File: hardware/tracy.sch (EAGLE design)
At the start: 62 parts, among them IC1 SIM900, J1 U.FL, Q1 si2305cd, Q2 8MHz 18pF, Q3 IRFR5305, T1 BC846, U1 SPX5205 3v3, X3 MKDSN1,5/4-5,08, Y1 32768Hz CFPX-217 12.5pF

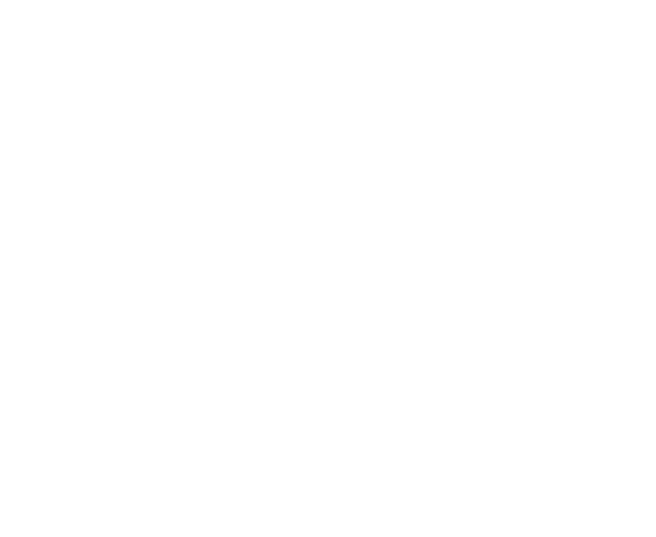
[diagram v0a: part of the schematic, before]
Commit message: create sim card reader footprint
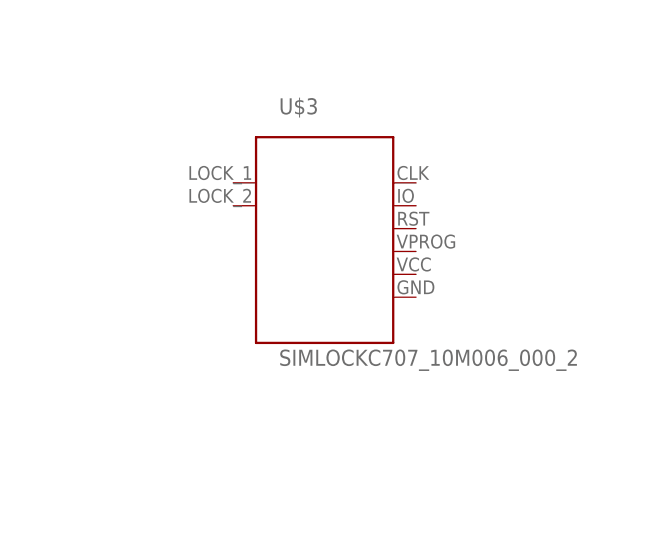
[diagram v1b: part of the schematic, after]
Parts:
- added U$3: SIMLOCKC707_10M006_000_2, Simplex-Connectors:SIMLOCKC707_10M006_000_2
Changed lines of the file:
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@@
 <part name="GND8" library="SparkFun" deviceset="GND" device=""/>
 <part name="IC1" library="sim900" deviceset="SIM900" device=""/>
+<part name="U$3" library="Simplex-Connectors" deviceset="SIMLOCK" device="C707_10M006_000_2"/>
 </parts>
 <sheets>
@@
 <instance part="GND8" gate="1" x="22.86" y="241.3"/>
 <instance part="IC1" gate="G$1" x="345.44" y="363.22"/>
+<instance part="U$3" gate="G$1" x="441.96" y="378.46"/>
 </instances>
 <busses>

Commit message: sch work
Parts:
- removed C15: 10uF, SparkFun-Capacitors:CAP_POLD
- removed C2, C20: 10uF, rcl:C-EUC1206
- removed C21, C22: 33pF, rcl:C-EUC0805
- removed D2: SB560, diode:DIODE-C1702-05
- removed JP1: i2c, SparkFun-Connectors:M04PTH
- removed JP2: thermistor, SparkFun-Connectors:M02PTH
- removed JP5: debug, SparkFun-Connectors:M07
- removed JP9: digital2, SparkFun-Connectors:M07
- removed LED1: green, led:LEDCHIP-LED0805
- removed LED2: orange, led:LEDCHIP-LED0805
- removed Q1: si2305cd, Simplex-DiscreteSemi:MOSFET-PCHANNELSMD_POWER
- removed Q2: 8MHz 18pF, Omat_komponentit:CRYTAL
- removed Q3: IRFR5305, transistor-power:IRFR5305
- removed R10, R27: 1K, rcl:R-EU_R0805W
- removed R12, R13: 320, rcl:R-EU_R0805W
- removed R16, R3: 100k, rcl:R-EU_R0805W
- removed R19, R8: 10k, rcl:R-EU_R0805W
- removed R25: 2M, rcl:R-EU_R0805W
- removed R26: 240k, rcl:R-EU_R0805W
- removed R4, R5, R6, R7: 4.7k, rcl:R-EU_R0805W
- removed T1: BC846, transistor:BC846
- removed U$4: INDUCTOR, Simplex-rlc:INDUCTOR
- removed X3: MKDSN1,5/4-5,08, con-phoenix-508:MKDSN1,5/4-5,08
- added C12: 4u7, rcl:C-EUC0805
- added C13: 100n, rcl:C-EUC0805
- added C14: 22p, rcl:C-EUC0805
- added C16: 47uF, rcl:C-EUC1206
- added C25, C26, C29: 100nF, rcl:C-EUC0805
- added C27, C28: 4u7, rcl:C-EUC1206
- added C30: 10uF, rcl:C-EUC1206
- added C32: 1uF, rcl:C-EUC0805
- added D1: DIODE-SCHOTTKY_, SparkFun-DiscreteSemi:DIODE-SCHOTTKY_
- added J2: U.FL, SparkFun-Connectors:U.FL
- added LED3: orange, led:LEDCHIP-LED0805
- added Q4: si2305cd, Simplex-DiscreteSemi:MOSFET-PCHANNELSMD_POWER
- added R11: 3k, rcl:R-EU_R0805W
- added R14: NA/10k, rcl:R-EU_R0805W
- added R15: 1k1, rcl:R-EU_R0805W
- added R17, R23, R9: 10k, rcl:R-EU_R0805W
- added R18: 47k, rcl:R-EU_R0805W
- added R20: 4k7, rcl:R-EU_R0805W
- added R21: 100k, rcl:R-EU_R0805W
- added T2: BC846, transistor:BC846
- added U$10: bead, Simplex-rlc:INDUCTOR
- added U$6: BQ24072, Simplex-ICs:BQ24072
- added U$8: 22, Simplex-rlc:RES_ARR
- added U$9: RESETTABLE, Simplex-Fuses:RESETTABLE
- added U3: TC1014 2V8, SparkFun:V_REG_LDOSMD
- C19: value 100nF -> 10uF; device rcl:C-EUC0805 -> rcl:C-EUC1206
- R2: value 10k -> 470
- U$2: value RESETTABLE -> 470; device Simplex-Fuses:RESETTABLE -> Simplex-rlc:RES_ARR
- U$5: value INDUCTOR -> bead
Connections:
- net CS renamed P4.6
- net MOSI renamed P4.1
- removed net EN: R8.1, U$1.20
- removed net LED: R10.2, U$1.36
- removed net MISO: U$1.31
- removed net N$11: R6.2, U$1.34
- removed net N$12: R13.1, U2.TX
- removed net N$13: R7.2, U$1.33
- removed net N$14: Q1.G, R3.1, R8.2
- removed net N$15: U$5.1
- removed net N$16: R12.1, U2.RX
- removed net N$17: C22.2, Q2.1, U$1.46
- removed net N$18: R13.2
- removed net N$19: R12.2
- removed net N$23: C21.2, Q2.2, U$1.45
- removed net N$28: Q3.G, R2.2
- removed net N$37: Q1.D, U$4.1
- removed net N$39: LED2.C, R27.2
- removed net PU.0: U$1.38
- removed net PU.1: U$1.40
- removed net PUR: U$1.39
- removed net PV+: Q3.S, R19.1, R22.1, X3-4.KL
- removed net RX: JP5.5, R6.1
- removed net SCK: LED2.A, U$1.32
- removed net SCL: JP1.1, R4.2, U$1.3
- removed net SDA: JP1.2, R5.2, U$1.4
- removed net SENSE: D2.A, Q3.D
- removed net TX: JP5.6, R7.1
- removed net VBAT_GND: JP2.1, X3-1.KL, X3-2.KL
- removed net VBUS: U$1.41
- removed net VCC: C17.2, C8.2, C9.2, JP5.4, Q1.S, R3.2, R34.2, U$1.11, U$1.28, U$1.7
- removed net VCC_EN: C20.1, JP1.3, JP9.6, R4.1, R5.1, U$4.2
- removed net VUSB: U$1.42
- new net 2V8: C17.2, C29.1, C30.1, C8.2, C9.2, R34.2, U$1.11, U$1.28, U$1.7, U3.OUT
- new net 3V3_EN: U1.EN
- new net 5V: U$9.P$1
- new net 5V_IN: D1.C, R22.1, U$6.IN
- new net BAT: C27.1, U$6.BAT
- new net CE: U$6.CE
- new net CTS: IC1G$1.CTS
- new net DTR: IC1G$1.DTR
- new net GPRS_EN: R23.1
- new net GPRS_POW: R20.2
- new net GPRS_RX: IC1G$1.RXD, U$2.7
- new net GPRS_TX: IC1G$1.TXD, U$2.8
- new net GPS_RX: U$2.5, U2.RX
- new net GPS_TX: R2.1, U$2.6, U2.TX
- new net N$20: D1.A, U$9.P$2
- new net N$21: LED3.C, U$6.CHG
- new net N$22: LED3.A, R9.2
- new net N$27: R11.1, U$6.ISET
- new net N$29: R14.1, U$6.TS
- new net N$30: C12.2, IC1G$1.VRTC
- new net N$32: C13.2, IC1G$1.SIM_VDD, U$3.VCC
- new net N$33: R15.1, U$6.ILIM
- new net N$34: U$3.CLK, U$8.1
- new net N$35: U$3.RST, U$8.3
- new net N$36: U$3.IO, U$8.2
- new net N$38: IC1G$1.SIM_CLK, U$8.8
- new net N$40: IC1G$1.SIM_RST, U$8.6
- new net N$41: C14.2, IC1G$1.SIM_DATA, U$8.7
- new net N$42: IC1G$1.SIM_PRESENCE, R17.2, U$3.LOCK_01
- new net N$43: IC1G$1.VDD_EXT, R17.1
- new net N$44: IC1G$1.PWRKEY, T2.C
- new net N$45: R18.2, R20.1, T2.B
- new net N$46: IC1G$1.RF_ANT, J2.SIGNAL
- new net N$48: Q4.G, R21.1, R23.2
- new net N$49: Q4.D, U$10.1
- new net N$50: C32.1, U3.BP
- new net P4.7: U$1.36
- new net P6.2: U$1.3
- new net P6.3: U$1.4
- new net RI: IC1G$1.RI
- new net RTS: IC1G$1.RTS
- net +3V3: now also U$5.1; no longer C2.1
- net GND: now also C12.1, C13.1, C14.1, C16.2, C25.2, C26.2, C27.2, C28.2, C29.2, C30.2, C32.2, J2.GND@0, J2.GND@1, R11.2, R14.2, R15.2, R18.1, R2.2, T2.E, U$3.GND, U$3.LOCK_02, U$6.EN1, U$6.TD, U$6.VSS, U3.GND; no longer C2.2, C20.2, C21.1, C22.1, JP1.4, JP5.1, JP5.7, JP9.7, LED1.C, R26.2, R27.1, T1.E
- net N$1: now also U$1.32, U$2.3; no longer LED1.A, R10.1
- net N$3: now also U$1.31, U$2.4; no longer R16.1, T1.B
- net N$4: now also U$1.33, U$2.2; no longer D2.C
- net N$5: now also U$1.34, U$2.1; no longer R19.2, R2.1, T1.C
- net P1.0: no longer JP9.1
- net P1.1: no longer JP9.2
- net P1.2: no longer JP9.3
- net P1.3: no longer JP9.4
- net P2.0: now also U$1.20; no longer R16.2
- net P4.0: no longer JP9.5
- net P5.0: no longer JP2.2
- net P6.0: no longer C19.1, R25.2, R26.1
- net RST: no longer JP5.2
- net TEST: no longer JP5.3
- net VBAT: now also C16.1, C19.1, C25.1, C26.1, U$10.2; no longer R25.1, U$2.P$1, X3-3.KL
- net VIN: now also C28.1, Q4.S, R21.2, R9.1, U$6.EN2, U$6.OUT, U3.EN, U3.IN; no longer U$2.P$2, U1.EN
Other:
- note added: "add smf05c"
- note added: "digital output pins: - CE (LiPo charge enable) - 3V3_EN - GPRS_EN - VBACKUP (GPS)"
- moved on the sheet: C18, C19, R2, R22, R24, U$3

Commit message: daily snapshot
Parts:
- removed C16: 47uF, rcl:C-EUC1206
- removed C25: 100nF, rcl:C-EUC0805
- added C2: 100nF, rcl:C-EUC0805
- added R3: 2M, rcl:R-EU_R0805W
- added R4: 240k, rcl:R-EU_R0805W
- added R5: 4k7, rcl:R-EU_R0805W
- added U$17: battery, Simplex-Connectors:MOLEX_40530480410
- added U$18: 22, Simplex-rlc:RES_ARR
- added U$19: power_in, Simplex-Connectors:MOLEX_40530480410
- added U$20: debug, Simplex-Connectors:MOLEX_6VERTICAL
- C18: value 100nF -> NA 100nF
- C19: value 10uF -> 47uF
- U$8: value 22 -> SMF05C; device Simplex-rlc:RES_ARR -> Simplex-DiscreteSemi:SMF05C
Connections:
- removed net N$29: R14.1, U$6.TS
- removed net N$38: IC1G$1.SIM_CLK, U$8.8
- removed net N$40: IC1G$1.SIM_RST, U$8.6
- removed net N$41: C14.2, IC1G$1.SIM_DATA, U$8.7
- new net N$10: IC1G$1.STATUS
- new net N$11: IC1G$1.NETLIGHT\
- new net N$12: R5.1, U$19.2
- new net N$17: IC1G$1.SIM_DATA, U$18.8
- new net N$18: IC1G$1.SIM_CLK, U$18.7
- new net N$19: IC1G$1.SIM_RST, U$18.6
- new net PW_EN: R5.2
- new net PW_RAW: R22.1, U$19.1
- new net TS: R14.1, U$17.1, U$6.TS
- net 2V8: now also U$20.4
- net 5V: now also U$19.4
- net 5V_IN: no longer R22.1
- net BAT: now also R3.1, U$17.4
- net GND: now also C2.2, R4.2, U$17.2, U$17.3, U$19.3, U$20.1, U$8.ANODE; no longer C16.2, C25.2
- net N$32: now also U$8.CATODE2
- net N$34: now also U$18.2, U$8.CATODE3; no longer U$8.1
- net N$35: now also U$18.3, U$8.CATODE5; no longer U$8.3
- net N$36: now also C14.2, U$18.1, U$8.CATODE4; no longer U$8.2
- net N$42: now also U$8.CATODE1
- net P4.0: now also U$20.6
- net P4.1: now also U$20.5
- net P6.2: now also C2.1, R3.2, R4.1
- net RST: now also U$20.2
- net TEST: now also U$20.3
- net VBAT: no longer C16.1, C25.1
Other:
- note added: "digital output pins: - CE (LiPo charge enable) - 3V3_EN - GPRS_EN - VBACKUP (GPS) - PW_EN"
- note removed: "add smf05c"
- note removed: "digital output pins: - CE (LiPo charge enable) - 3V3_EN - GPRS_EN - VBACKUP (GPS)"

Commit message: daily snapshot
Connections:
- net N$30 renamed VRTC
- net N$32 renamed SIM_VCC
- net N$34 renamed SIMLOCK_CLK
- net N$35 renamed SIMLOCK_RST
- net N$36 renamed SIMLOCK_IO
- net N$44 renamed PWRKEY
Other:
- note added: "digital input pins: - RI (detect incoming sms) - CTS"
- note added: "digital output pins: - CE (LiPo charge enable) - 3V3_EN - GPRS_EN - VBACKUP (GPS) - PW_EN - DTR (wake up gprs) - RTS"
- note removed: "digital output pins: - CE (LiPo charge enable) - 3V3_EN - GPRS_EN - VBACKUP (GPS) - PW_EN"
- moved on the sheet: C1, C10, C11, C12, C13, C14, C17, C18, C19, C2, C23, C24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

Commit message: daily snapshot
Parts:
- IC1: device sim900:SIM900 -> Simplex-ICs:SIM900
- R2: value 470 -> 2k2
- U$20: value debug -> MOLEX_6VERTICAL
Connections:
- removed net N$10: IC1G$1.STATUS
- removed net N$11: IC1G$1.NETLIGHT\
- new net P1.6: U$1.20
- net 5V_IN: now also U$6G$1.IN; no longer U$6.IN
- net BAT: now also U$6G$1.BAT; no longer U$6.BAT
- net CE: now also U$6G$1.CE; no longer U$6.CE
- net GND: now also R2.1, U$6G$1.EN1, U$6G$1.TD, U$6G$1.VSS, U$6TH.TH; no longer R2.2, U$6.EN1, U$6.TD, U$6.VSS
- net GPS_TX: no longer R2.1
- net N$21: now also U$6G$1.CHG; no longer U$6.CHG
- net N$27: now also U$6G$1.ISET; no longer U$6.ISET
- net N$33: now also U$6G$1.ILIM; no longer U$6.ILIM
- net N$5: now also R2.2
- net P2.0: no longer U$1.20
- net TS: now also U$6G$1.TS; no longer U$6.TS
- net VIN: now also U$6G$1.EN2, U$6G$1.OUT; no longer U$6.EN2, U$6.OUT
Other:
- moved on the sheet: R2

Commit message: pcb done
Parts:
- removed LED3: orange, led:LEDCHIP-LED0805
- removed R9: 10k, rcl:R-EU_R0805W
- added LED1: green, led:LEDCHIPLED_0805
- added R6: 100k, rcl:R-EU_R0805W
- added R7: 470, rcl:R-EU_R0805W
- R14: value NA/10k -> DNP 10k th
- U$17: value battery -> MOLEX_4HORIZONTAL; device Simplex-Connectors:MOLEX_40530480410 -> Simplex-Connectors:MOLEX_4HORIZONTAL
- U$19: value power_in -> MOLEX_4HORIZONTAL; device Simplex-Connectors:MOLEX_40530480410 -> Simplex-Connectors:MOLEX_4HORIZONTAL
- U2: value (none) -> 3339
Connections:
- net N$8 renamed GPS_VCC
- removed net N$21: LED3.C, U$6G$1.CHG
- removed net N$22: LED3.A, R9.2
- removed net P1.0: U$1.14
- removed net P1.1: U$1.15
- removed net P1.2: U$1.16
- removed net P1.3: U$1.17
- removed net P1.4: U$1.18
- removed net P1.5: U$1.19
- removed net P1.6: U$1.20
- removed net P1.7: U$1.21
- removed net P2.0: U$1.22
- removed net P4.6: U$1.35
- removed net P4.7: U$1.36
- removed net P5.0: U$1.5
- removed net P5.1: U$1.6
- removed net P6.0: U$1.1
- removed net P6.1: C18.1, R22.2, R24.1, U$1.2
- removed net P6.2: C2.1, R3.2, R4.1, U$1.3
- removed net P6.3: U$1.4
- new net BAT_DIV: C2.1, R3.2, R4.1, U$1.4
- new net CH: R7.2, U$1.15
- new net N$10: R7.1, U$6G$1.CHG
- new net N$8: LED1.C, R6.1
- new net PW_RAW_DIV: C18.1, R22.2, R24.1, U$1.3
- new net STATUS: LED1.A, U$1.16
- net 3V3_EN: now also U$1.1
- net 5V: now also U$17.4; no longer U$19.4
- net BAT: now also U$19.1; no longer U$17.4
- net CE: now also U$1.2
- net CTS: now also U$1.19
- net DTR: now also U$1.17
- net GND: now also R6.2, U$19.2; no longer U$17.2
- net GPRS_EN: now also U$1.21
- net GPRS_POW: now also U$1.22
- net N$12: now also U$17.2; no longer U$19.2
- net P4.0: now also U$20.5; no longer U$20.6
- net P4.1: now also U$20.6; no longer U$20.5
- net PW_EN: now also U$1.36
- net PW_RAW: now also U$17.1; no longer U$19.1
- net RI: now also U$1.18
- net RTS: now also U$1.20
- net TS: now also U$19.4; no longer U$17.1
- net VBACKUP: now also U$1.35
- net VIN: no longer R9.1
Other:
- note added: "digital input pins: - RI (detect incoming sms) - CTS - ^CH (LiPo charging)"
- note added: "digital output pins: - CE (LiPo charge enable) - 3V3_EN - GPRS_EN - GPRS_POW - VBACKUP (GPS) - PW_EN - DTR (wake up gprs) - RTS"
- note removed: "digital input pins: - RI (detect incoming sms) - CTS"
- note removed: "digital output pins: - CE (LiPo charge enable) - 3V3_EN - GPRS_EN - VBACKUP (GPS) - PW_EN - DTR (wake up gprs) - RTS"
- moved on the sheet: C10, U$17, U$19
